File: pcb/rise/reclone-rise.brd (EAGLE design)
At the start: 85 x 56 mm, 12 parts, among them J1 MAGJACK, U1 6SLX25FTG256

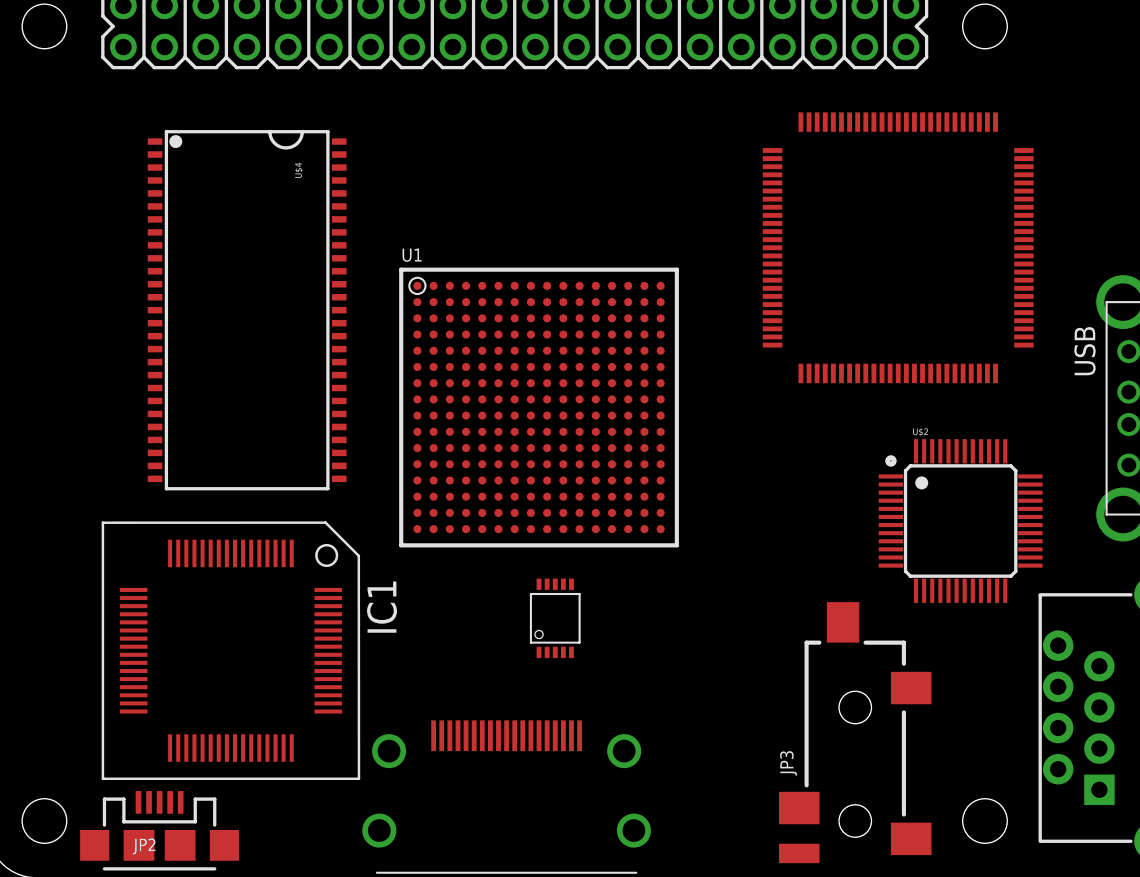
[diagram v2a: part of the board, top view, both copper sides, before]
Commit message: Rearranged and rotated some components to find a possible fit
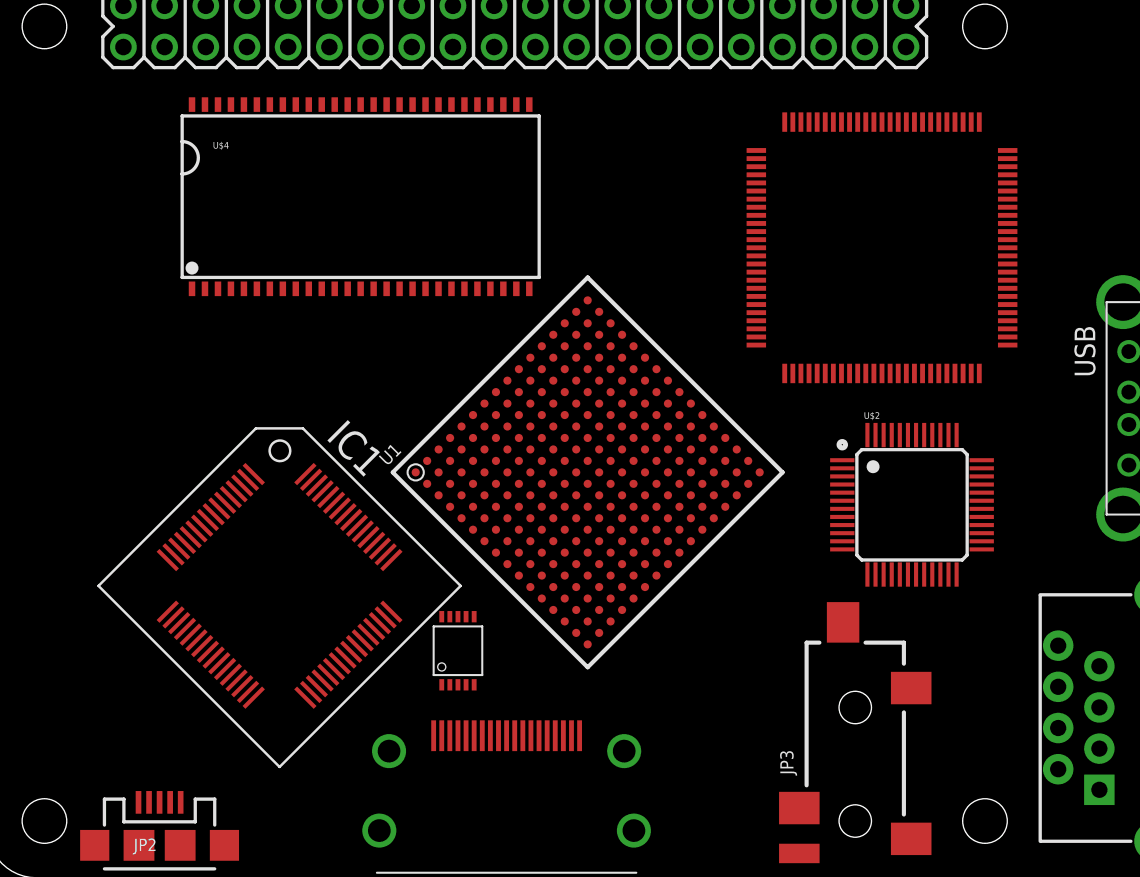
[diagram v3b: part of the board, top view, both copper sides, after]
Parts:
- moved U$4 9.90 mm to (23.0, 42.0), turned to 0 degrees
- moved U$1 6.32 mm to (29.0, 14.0)
- moved IC1 5.00 mm to (18.0, 18.0), turned to 225 degrees
- moved U1 5.00 mm to (37.0, 25.0), turned to 45 degrees
- moved U$2 3.16 mm to (57.0, 23.0)
- moved MCU 1.00 mm to (48.0, 46.0)
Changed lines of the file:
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@@
 <elements>
 <element name="USB" library="reclone-rise" package="USB-A-2H" value="USB_A_2H" x="69" y="29" rot="R180"/>
-<element name="MCU" library="reclone-rise" package="LQFP-100" value="STM32F407VGT6" x="49" y="46" rot="R270"/>
-<element name="U1" library="xilinx_devices_V6" package="FT256" value="6SLX25FTG256" x="34" y="29"/>
+<element name="MCU" library="reclone-rise" package="LQFP-100" value="STM32F407VGT6" x="48" y="46" rot="R270"/>
+<element name="U1" library="xilinx_devices_V6" package="FT256" value="6SLX25FTG256" x="37" y="25" rot="R45"/>
 <element name="JP1" library="SparkFun-Connectors" package="2X20" value="M20X2" x="32.5" y="52.5"/>
 <element name="J1" library="SparkFun-Connectors" package="MAGJACK" value="MAGJACK" x="86" y="2.25" rot="R90"/>
-<element name="IC1" library="ftdichip-3" package="TQFP64-12X12" value="" x="15" y="14" rot="R180"/>
+<element name="IC1" library="ftdichip-3" package="TQFP64-12X12" value="" x="18" y="18" rot="R225"/>
 <element name="JP2" library="SparkFun-Connectors" package="USB-MICROB" value="USB-MICROB" x="10.6" y="2">
 <attribute name="PROD_ID" value="CONN-09505" x="10.6" y="2" size="1.778" layer="27" display="off"/>
@@
 <attribute name="PROD_ID" value="CONN-10353" x="53.5" y="0" size="1.778" layer="27" rot="R90" display="off"/>
 </element>
-<element name="U$1" library="reclone-rise" package="TSSOP10" value="PCA9527" x="35" y="16" rot="R90"/>
-<element name="U$2" library="reclone-rise" package="LQFP-48" value="DP83848C" x="60" y="22"/>
+<element name="U$1" library="reclone-rise" package="TSSOP10" value="PCA9527" x="29" y="14" rot="R90"/>
+<element name="U$2" library="reclone-rise" package="LQFP-48" value="DP83848C" x="57" y="23"/>
 <element name="U$3" library="reclone-rise" package="HDMI_A_SMT" value="HDMI_A" x="32" y="4" rot="R270"/>
-<element name="U$4" library="reclone-rise" package="TSOP54-400" value="MT48LC16M16A2P" x="16" y="35" rot="R270"/>
+<element name="U$4" library="reclone-rise" package="TSOP54-400" value="MT48LC16M16A2P" x="23" y="42"/>
 </elements>
 <signals>
@@
 <contactref element="IC1" pad="47"/>
 <contactref element="IC1" pad="51"/>
-<wire x1="38.5" y1="33.5" x2="41.5" y2="36.5" width="0" layer="19" extent="1-1"/>
-<wire x1="36.5" y1="35.5" x2="38.5" y2="33.5" width="0" layer="19" extent="1-1"/>
-<wire x1="40.5" y1="30.5" x2="38.5" y2="33.5" width="0" layer="19" extent="1-1"/>
-<wire x1="37.5" y1="29.5" x2="40.5" y2="30.5" width="0" layer="19" extent="1-1"/>
-<wire x1="34.5" y1="29.5" x2="37.5" y2="29.5" width="0" layer="19" extent="1-1"/>
-<wire x1="33.5" y1="30.5" x2="34.5" y2="29.5" width="0" layer="19" extent="1-1"/>
-<wire x1="32.5" y1="29.5" x2="33.5" y2="30.5" width="0" layer="19" extent="1-1"/>
-<wire x1="33.5" y1="28.5" x2="34.5" y2="29.5" width="0" layer="19" extent="1-1"/>
-<wire x1="34.5" y1="27.5" x2="33.5" y2="28.5" width="0" layer="19" extent="1-1"/>
-<wire x1="32.5" y1="27.5" x2="33.5" y2="28.5" width="0" layer="19" extent="1-1"/>
-<wire x1="34.5" y1="32.5" x2="33.5" y2="30.5" width="0" layer="19" extent="1-1"/>
-<wire x1="30.5" y1="28.5" x2="32.5" y2="29.5" width="0" layer="19" extent="1-1"/>
-<wire x1="33.5" y1="25.5" x2="34.5" y2="27.5" width="0" layer="19" extent="1-1"/>
-<wire x1="32.5" y1="35.5" x2="34.5" y2="32.5" width="0" layer="19" extent="1-1"/>
-<wire x1="29.5" y1="33.5" x2="32.5" y2="35.5" width="0" layer="19" extent="1-1"/>
-<wire x1="27.5" y1="30.5" x2="30.5" y2="28.5" width="0" layer="19" extent="1-1"/>
-<wire x1="35.5" y1="22.5" x2="33.5" y2="25.5" width="0" layer="19" extent="1-1"/>
-<wire x1="38.5" y1="24.5" x2="35.5" y2="22.5" width="0" layer="19" extent="1-1"/>
-<wire x1="40.5" y1="26.5" x2="38.5" y2="24.5" width="0" layer="19" extent="1-1"/>
-<wire x1="31.5" y1="22.5" x2="33.5" y2="25.5" width="0" layer="19" extent="1-1"/>
-<wire x1="28.5" y1="23.5" x2="31.5" y2="22.5" width="0" layer="19" extent="1-1"/>
-<wire x1="26.5" y1="21.5" x2="28.5" y2="23.5" width="0" layer="19" extent="1-1"/>
-<wire x1="27.5" y1="26.5" x2="28.5" y2="23.5" width="0" layer="19" extent="1-1"/>
-<wire x1="26.5" y1="36.5" x2="29.5" y2="33.5" width="0" layer="19" extent="1-1"/>
-<wire x1="41.5" y1="21.5" x2="38.5" y2="24.5" width="0" layer="19" extent="1-1"/>
-<wire x1="18.2501" y1="7.9999" x2="26.5" y2="21.5" width="0" layer="19" extent="1-1"/>
-<wire x1="21.0001" y1="11.25" x2="18.2501" y2="7.9999" width="0" layer="19" extent="1-1"/>
-<wire x1="12.2499" y1="7.9999" x2="18.2501" y2="7.9999" width="0" layer="19" extent="1-1"/>
-<wire x1="8.9999" y1="13.75" x2="12.2499" y2="7.9999" width="0" layer="19" extent="1-1"/>
-<wire x1="11.75" y1="20.0001" x2="8.9999" y2="13.75" width="0" layer="19" extent="1-1"/>
-<wire x1="13.75" y1="20.0001" x2="11.75" y2="20.0001" width="0" layer="19" extent="1-1"/>
-<wire x1="16.75" y1="20.0001" x2="13.75" y2="20.0001" width="0" layer="19" extent="1-1"/>
-<wire x1="18.75" y1="20.0001" x2="16.75" y2="20.0001" width="0" layer="19" extent="1-1"/>
+<wire x1="37" y1="31.363959375" x2="37" y2="35.6066" width="0" layer="19" extent="1-1"/>
+<wire x1="34.171571875" y1="31.363959375" x2="37" y2="31.363959375" width="0" layer="19" extent="1-1"/>
+<wire x1="40.53553125" y1="30.656853125" x2="37" y2="31.363959375" width="0" layer="19" extent="1-1"/>
+<wire x1="39.12131875" y1="27.828425" x2="40.53553125" y2="30.656853125" width="0" layer="19" extent="1-1"/>
+<wire x1="37" y1="25.70710625" x2="39.12131875" y2="27.828425" width="0" layer="19" extent="1-1"/>
+<wire x1="35.585784375" y1="25.70710625" x2="37" y2="25.70710625" width="0" layer="19" extent="1-1"/>
+<wire x1="35.585784375" y1="24.292890625" x2="35.585784375" y2="25.70710625" width="0" layer="19" extent="1-1"/>
+<wire x1="37" y1="24.292890625" x2="37" y2="25.70710625" width="0" layer="19" extent="1-1"/>
+<wire x1="38.4142125" y1="24.292890625" x2="37" y2="24.292890625" width="0" layer="19" extent="1-1"/>
+<wire x1="37" y1="22.878678125" x2="37" y2="24.292890625" width="0" layer="19" extent="1-1"/>
+<wire x1="34.878678125" y1="27.828425" x2="35.585784375" y2="25.70710625" width="0" layer="19" extent="1-1"/>
+<wire x1="34.878678125" y1="22.171571875" x2="35.585784375" y2="24.292890625" width="0" layer="19" extent="1-1"/>
+<wire x1="39.12131875" y1="22.171571875" x2="38.4142125" y2="24.292890625" width="0" layer="19" extent="1-1"/>
+<wire x1="31.34314375" y1="28.53553125" x2="34.878678125" y2="27.828425" width="0" layer="19" extent="1-1"/>
+<wire x1="30.6360375" y1="25" x2="31.34314375" y2="28.53553125" width="0" layer="19" extent="1-1"/>
+<wire x1="31.34314375" y1="21.464465625" x2="34.878678125" y2="22.171571875" width="0" layer="19" extent="1-1"/>
+<wire x1="42.656853125" y1="21.464465625" x2="39.12131875" y2="22.171571875" width="0" layer="19" extent="1-1"/>
+<wire x1="43.363959375" y1="25" x2="42.656853125" y2="21.464465625" width="0" layer="19" extent="1-1"/>
+<wire x1="43.363959375" y1="27.828425" x2="43.363959375" y2="25" width="0" layer="19" extent="1-1"/>
+<wire x1="39.828425" y1="18.6360375" x2="39.12131875" y2="22.171571875" width="0" layer="19" extent="1-1"/>
+<wire x1="37" y1="17.221825" x2="39.828425" y2="18.6360375" width="0" layer="19" extent="1-1"/>
+<wire x1="37" y1="14.393396875" x2="37" y2="17.221825" width="0" layer="19" extent="1-1"/>
+<wire x1="34.171571875" y1="18.6360375" x2="37" y2="17.221825" width="0" layer="19" extent="1-1"/>
+<wire x1="26.393396875" y1="25" x2="30.6360375" y2="25" width="0" layer="19" extent="1-1"/>
+<wire x1="47.6066" y1="25" x2="43.363959375" y2="25" width="0" layer="19" extent="1-1"/>
+<wire x1="24.540878125" y1="16.05545625" x2="37" y2="14.393396875" width="0" layer="19" extent="1-1"/>
+<wire x1="24.187253125" y1="20.298165625" x2="24.540878125" y2="16.05545625" width="0" layer="19" extent="1-1"/>
+<wire x1="20.298096875" y1="11.812671875" x2="24.540878125" y2="16.05545625" width="0" layer="19" extent="1-1"/>
+<wire x1="13.9340625" y1="13.580509375" x2="20.298096875" y2="11.812671875" width="0" layer="19" extent="1-1"/>
+<wire x1="11.459190625" y1="19.9446125" x2="13.9340625" y2="13.580509375" width="0" layer="19" extent="1-1"/>
+<wire x1="12.873403125" y1="21.358825" x2="11.459190625" y2="19.9446125" width="0" layer="19" extent="1-1"/>
+<wire x1="14.994725" y1="23.480146875" x2="12.873403125" y2="21.358825" width="0" layer="19" extent="1-1"/>
+<wire x1="16.4089375" y1="24.894359375" x2="14.994725" y2="23.480146875" width="0" layer="19" extent="1-1"/>
 </signal>
 <signal name="AGND">
@@
 <contactref element="IC1" pad="37"/>
 <contactref element="IC1" pad="64"/>
-<wire x1="13.2501" y1="20.0001" x2="13.2499" y2="7.9999" width="0" layer="19" extent="1-1"/>
-<wire x1="21.0001" y1="17.7501" x2="13.2501" y2="20.0001" width="0" layer="19" extent="1-1"/>
+<wire x1="12.519921875" y1="21.00534375" x2="21.005203125" y2="12.519778125" width="0" layer="19" extent="1-1"/>
+<wire x1="19.5909875" y1="24.89443125" x2="12.519921875" y2="21.00534375" width="0" layer="19" extent="1-1"/>
 </signal>
 <signal name="VCCIO">
@@
 <contactref element="IC1" pad="42"/>
 <contactref element="IC1" pad="56"/>
-<wire x1="8.9999" y1="16.2499" x2="8.9999" y2="10.7531" width="0" layer="19" extent="1-1"/>
-<wire x1="15.75" y1="7.9999" x2="8.9999" y2="10.7531" width="0" layer="19" extent="1-1"/>
-<wire x1="21.0001" y1="13.7499" x2="15.75" y2="7.9999" width="0" layer="19" extent="1-1"/>
+<wire x1="12.16636875" y1="15.34820625" x2="16.053190625" y2="11.46138125" width="0" layer="19" extent="1-1"/>
+<wire x1="22.773040625" y1="14.287615625" x2="16.053190625" y2="11.46138125" width="0" layer="19" extent="1-1"/>
+<wire x1="22.41955625" y1="22.0658625" x2="22.773040625" y2="14.287615625" width="0" layer="19" extent="1-1"/>
 </signal>
 <signal name="VPLL">

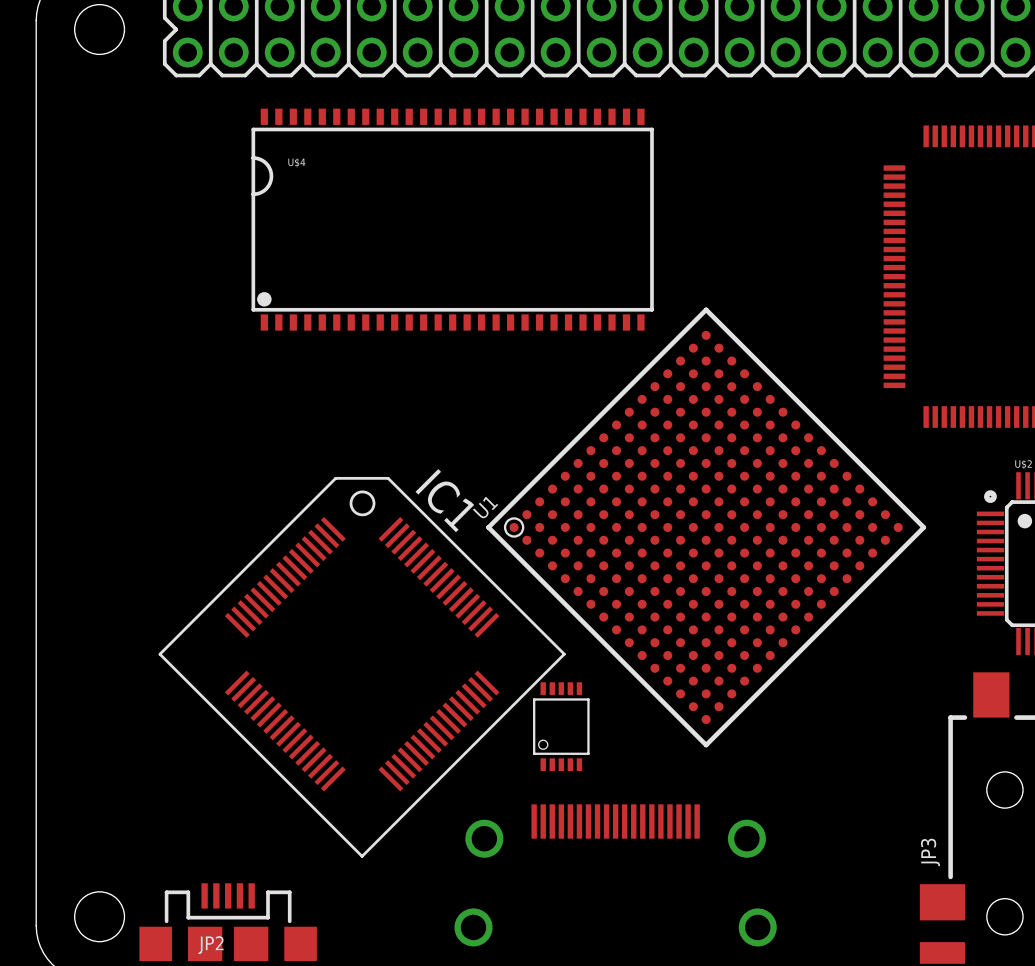
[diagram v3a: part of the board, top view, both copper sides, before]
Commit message: Added rectangle to help plan for the size of a DDR2 chip
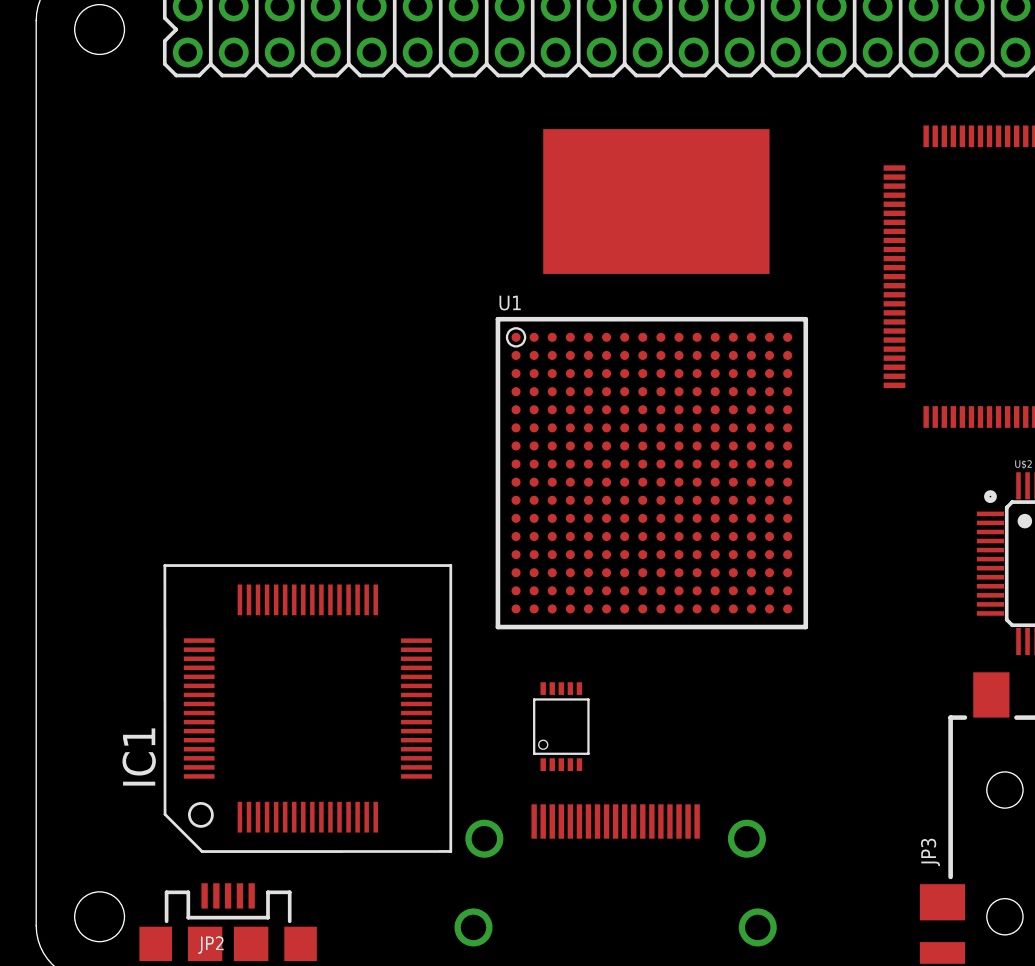
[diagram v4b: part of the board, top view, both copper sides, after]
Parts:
- removed U$4: MT48LC16M16A2P, reclone-rise:TSOP54-400
- moved IC1 4.24 mm to (15.0, 15.0), turned to 0 degrees
- moved U1 4.24 mm to (34.0, 28.0), turned to 0 degrees
